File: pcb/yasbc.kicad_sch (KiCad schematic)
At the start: 173 parts, among them J1 BOOT, J10 Conn_02x20_Odd_Even, J2 USB TTY, J3 AudioJack3, J4 1V5, J5 3V3, J6 1V2, J7 USB DEV, J8 Micro_SD_Card, J9 USB HOST, Q1 AO3401A, Q2 AO3401A, SW1 RESET, SW2 SW_SPDT, SW3 SW_SPDT, SW4 SW_SPDT, SW5 SW_SPDT, SW6 SW_5WAY, U1 BCT2028, U3 Allwinner_A13, U4 CH340E, U5 TD6810, U6 SE5120, U7 K4B4G1646E, U8 MPU-6050, Y1 24M

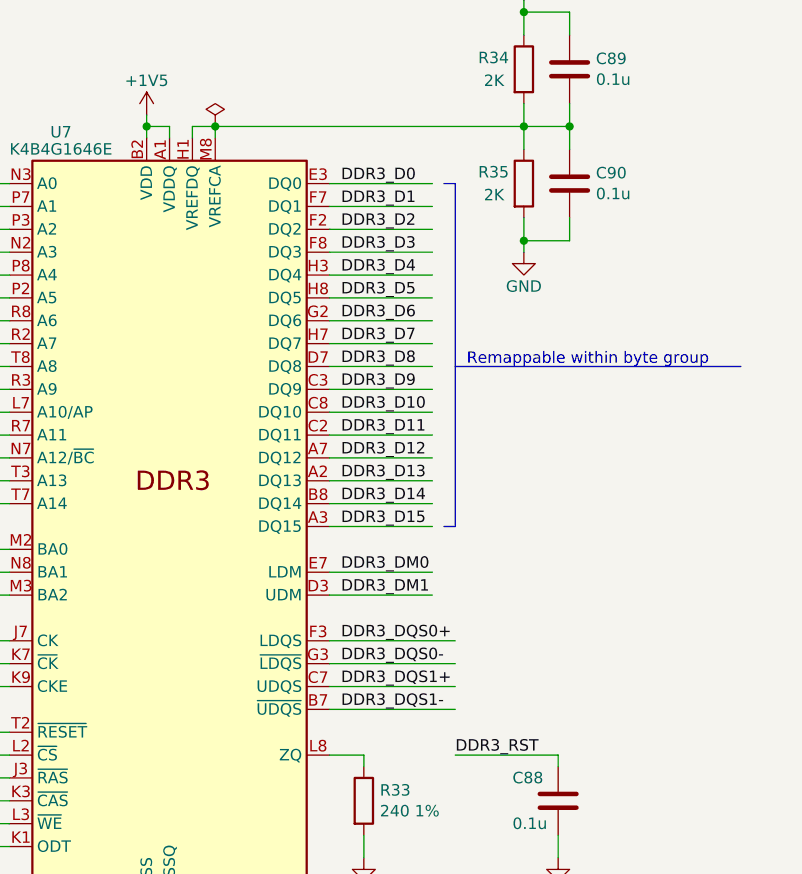
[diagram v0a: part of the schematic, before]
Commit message: Routed DDR3 data signals
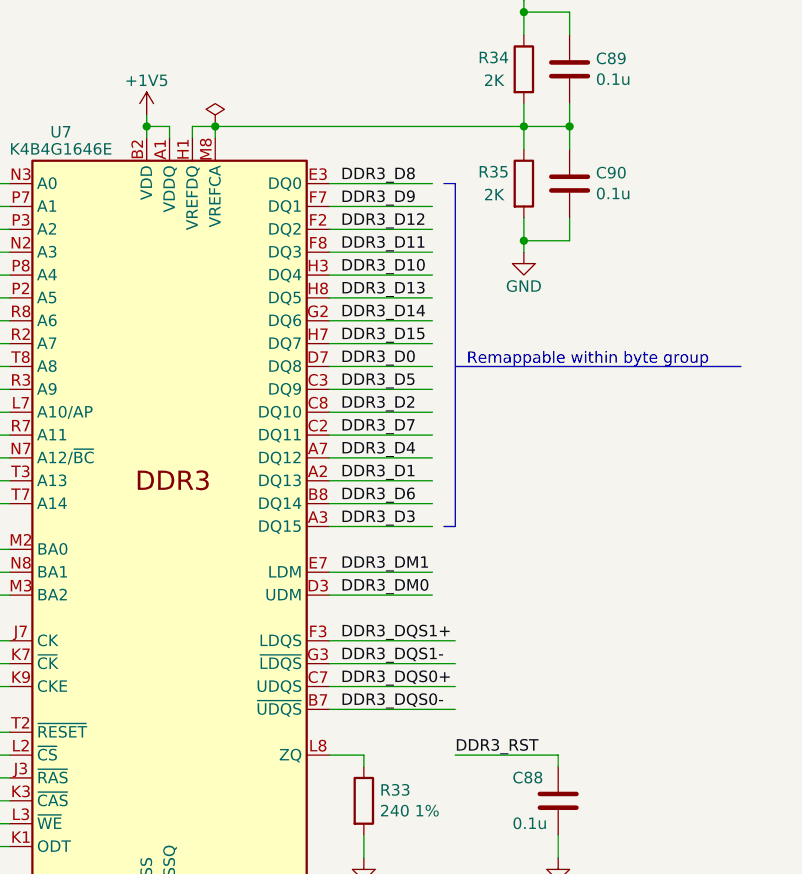
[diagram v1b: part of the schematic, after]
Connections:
- net DDR3_D0: now also U7.D7 (DQ8); no longer U7.E3 (DQ0)
- net DDR3_D1: now also U7.A2 (DQ13); no longer U7.F7 (DQ1)
- net DDR3_D10: now also U7.H3 (DQ4); no longer U7.C8 (DQ10)
- net DDR3_D11: now also U7.F8 (DQ3); no longer U7.C2 (DQ11)
- net DDR3_D12: now also U7.F2 (DQ2); no longer U7.A7 (DQ12)
- net DDR3_D13: now also U7.H8 (DQ5); no longer U7.A2 (DQ13)
- net DDR3_D14: now also U7.G2 (DQ6); no longer U7.B8 (DQ14)
- net DDR3_D15: now also U7.H7 (DQ7); no longer U7.A3 (DQ15)
- net DDR3_D2: now also U7.C8 (DQ10); no longer U7.F2 (DQ2)
- net DDR3_D3: now also U7.A3 (DQ15); no longer U7.F8 (DQ3)
- net DDR3_D4: now also U7.A7 (DQ12); no longer U7.H3 (DQ4)
- net DDR3_D5: now also U7.C3 (DQ9); no longer U7.H8 (DQ5)
- net DDR3_D6: now also U7.B8 (DQ14); no longer U7.G2 (DQ6)
- net DDR3_D7: now also U7.C2 (DQ11); no longer U7.H7 (DQ7)
- net DDR3_D8: now also U7.E3 (DQ0); no longer U7.D7 (DQ8)
- net DDR3_D9: now also U7.F7 (DQ1); no longer U7.C3 (DQ9)
- net DDR3_DM0: now also U7.D3 (UDM); no longer U7.E7 (LDM)
- net DDR3_DM1: now also U7.E7 (LDM); no longer U7.D3 (UDM)
- net DDR3_DQS0+: now also U7.C7 (UDQS); no longer U7.F3 (LDQS)
- net DDR3_DQS0-: now also U7.B7 (~{UDQS}); no longer U7.G3 (~{LDQS})
- net DDR3_DQS1+: now also U7.F3 (LDQS); no longer U7.C7 (UDQS)
- net DDR3_DQS1-: now also U7.G3 (~{LDQS}); no longer U7.B7 (~{UDQS})
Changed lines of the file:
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@@
   (no_connect (at 429.26 40.64))
   (no_connect (at 209.55 45.72))
-  (wire (pts (xy 533.4 71.12) (xy 544.83 71.12))
+  (wire (pts (xy 533.4 50.8) (xy 544.83 50.8))
     (stroke (width 0) (type default) (color 0 0 0 0))
   )
@@
     (stroke (width 0) (type default) (color 0 0 0 0))
   )
-  (wire (pts (xy 533.4 66.04) (xy 544.83 66.04))
+  (wire (pts (xy 533.4 45.72) (xy 544.83 45.72))
     (stroke (width 0) (type default) (color 0 0 0 0))
   )
@@
     (stroke (width 0) (type default) (color 0 0 0 0))
   )
-  (wire (pts (xy 533.4 96.52) (xy 547.37 96.52))
+  (wire (pts (xy 533.4 101.6) (xy 547.37 101.6))
     (stroke (width 0) (type default) (color 0 0 0 0))
   )
@@
     (stroke (width 0) (type default) (color 0 0 0 0))
   )
-  (wire (pts (xy 533.4 81.28) (xy 544.83 81.28))
+  (wire (pts (xy 533.4 60.96) (xy 544.83 60.96))
     (stroke (width 0) (type default) (color 0 0 0 0))
   )
@@
     (stroke (width 0) (type default) (color 0 0 0 0))
   )
-  (wire (pts (xy 533.4 60.96) (xy 544.83 60.96))
+  (wire (pts (xy 533.4 81.28) (xy 544.83 81.28))
     (stroke (width 0) (type default) (color 0 0 0 0))
   )
@@
     (stroke (width 0) (type default) (color 0 0 0 0))
   )
-  (wire (pts (xy 533.4 93.98) (xy 547.37 93.98))
+  (wire (pts (xy 533.4 99.06) (xy 547.37 99.06))
     (stroke (width 0) (type default) (color 0 0 0 0))
   )
@@
     (stroke (width 0) (type default) (color 0 0 0 0))
   )
-  (wire (pts (xy 533.4 55.88) (xy 544.83 55.88))
+  (wire (pts (xy 533.4 73.66) (xy 544.83 73.66))
     (stroke (width 0) (type default) (color 0 0 0 0))
   )
-  (wire (pts (xy 533.4 99.06) (xy 547.37 99.06))
+  (wire (pts (xy 533.4 93.98) (xy 547.37 93.98))
     (stroke (width 0) (type default) (color 0 0 0 0))
   )
@@
     (stroke (width 0) (type default) (color 0 0 0 0))
   )
-  (wire (pts (xy 533.4 78.74) (xy 544.83 78.74))
+  (wire (pts (xy 533.4 58.42) (xy 544.83 58.42))
     (stroke (width 0) (type default) (color 0 0 0 0))
   )
@@
     (stroke (width 0) (type default) (color 0 0 0 0))
   )
-  (wire (pts (xy 533.4 58.42) (xy 544.83 58.42))
+  (wire (pts (xy 533.4 78.74) (xy 544.83 78.74))
     (stroke (width 0) (type default) (color 0 0 0 0))
   )
@@
     (stroke (width 0) (type default) (color 0 0 0 0))
   )
-  (wire (pts (xy 533.4 76.2) (xy 544.83 76.2))
+  (wire (pts (xy 533.4 55.88) (xy 544.83 55.88))
     (stroke (width 0) (type default) (color 0 0 0 0))
   )
@@
     (stroke (width 0) (type default) (color 0 0 0 0))
   )
-  (wire (pts (xy 533.4 88.9) (xy 544.83 88.9))
+  (wire (pts (xy 533.4 86.36) (xy 544.83 86.36))
     (stroke (width 0) (type default) (color 0 0 0 0))
   )
@@
     (stroke (width 0) (type default) (color 0 0 0 0))
   )
-  (wire (pts (xy 533.4 48.26) (xy 544.83 48.26))
+  (wire (pts (xy 533.4 68.58) (xy 544.83 68.58))
     (stroke (width 0) (type default) (color 0 0 0 0))
   )
@@
     (stroke (width 0) (type default) (color 0 0 0 0))
   )
-  (wire (pts (xy 533.4 50.8) (xy 544.83 50.8))
+  (wire (pts (xy 533.4 71.12) (xy 544.83 71.12))
     (stroke (width 0) (type default) (color 0 0 0 0))
   )
@@
     (stroke (width 0) (type default) (color 0 0 0 0))
   )
-  (wire (pts (xy 533.4 101.6) (xy 547.37 101.6))
+  (wire (pts (xy 533.4 96.52) (xy 547.37 96.52))
     (stroke (width 0) (type default) (color 0 0 0 0))
   )
@@
     (stroke (width 0) (type default) (color 0 0 0 0))
   )
-  (wire (pts (xy 533.4 53.34) (xy 544.83 53.34))
+  (wire (pts (xy 533.4 76.2) (xy 544.83 76.2))
     (stroke (width 0) (type default) (color 0 0 0 0))
   )
@@
     (stroke (width 0) (type default) (color 0 0 0 0))
   )
-  (wire (pts (xy 533.4 45.72) (xy 544.83 45.72))
+  (wire (pts (xy 533.4 66.04) (xy 544.83 66.04))
     (stroke (width 0) (type default) (color 0 0 0 0))
   )
@@
     (stroke (width 0) (type default) (color 0 0 0 0))
   )
-  (wire (pts (xy 533.4 63.5) (xy 544.83 63.5))
+  (wire (pts (xy 533.4 43.18) (xy 544.83 43.18))
     (stroke (width 0) (type default) (color 0 0 0 0))
   )
@@
     (stroke (width 0) (type default) (color 0 0 0 0))
   )
-  (wire (pts (xy 533.4 68.58) (xy 544.83 68.58))
+  (wire (pts (xy 533.4 48.26) (xy 544.83 48.26))
     (stroke (width 0) (type default) (color 0 0 0 0))
   )
@@
     (stroke (width 0) (type default) (color 0 0 0 0))
   )
-  (wire (pts (xy 533.4 73.66) (xy 544.83 73.66))
+  (wire (pts (xy 533.4 53.34) (xy 544.83 53.34))
     (stroke (width 0) (type default) (color 0 0 0 0))
   )
@@
     (stroke (width 0) (type default) (color 0 0 0 0))
   )
-  (wire (pts (xy 533.4 43.18) (xy 544.83 43.18))
+  (wire (pts (xy 533.4 63.5) (xy 544.83 63.5))
     (stroke (width 0) (type default) (color 0 0 0 0))
   )
@@
     (stroke (width 0) (type default) (color 0 0 0 0))
   )
-  (wire (pts (xy 533.4 86.36) (xy 544.83 86.36))
+  (wire (pts (xy 533.4 88.9) (xy 544.83 88.9))
     (stroke (width 0) (type default) (color 0 0 0 0))
   )
@@
     (effects (font (size 1.27 1.27)) (justify left bottom))
   )
-  (label "DDR3_D13" (at 534.67 76.2 0)
+  (label "DDR3_D13" (at 534.67 55.88 0)
     (effects (font (size 1.27 1.27)) (justify left bottom))
   )
-  (label "DDR3_D3" (at 534.67 50.8 0)
+  (label "DDR3_D3" (at 534.67 81.28 0)
     (effects (font (size 1.27 1.27)) (justify left bottom))
   )
@@
     (effects (font (size 1.27 1.27)) (justify left bottom))
   )
-  (label "DDR3_D10" (at 534.67 68.58 0)
+  (label "DDR3_D10" (at 534.67 53.34 0)
     (effects (font (size 1.27 1.27)) (justify left bottom))
   )
@@
     (effects (font (size 1.27 1.27)) (justify left bottom))
   )
-  (label "DDR3_D2" (at 534.67 48.26 0)
+  (label "DDR3_D2" (at 534.67 68.58 0)
     (effects (font (size 1.27 1.27)) (justify left bottom))
   )
@@
     (effects (font (size 1.27 1.27)) (justify left bottom))
   )
-  (label "DDR3_D5" (at 534.67 55.88 0)
+  (label "DDR3_D5" (at 534.67 66.04 0)
     (effects (font (size 1.27 1.27)) (justify left bottom))
   )
@@
     (effects (font (size 1.27 1.27)) (justify left bottom))
   )
-  (label "DDR3_D4" (at 534.67 53.34 0)
+  (label "DDR3_D4" (at 534.67 73.66 0)
     (effects (font (size 1.27 1.27)) (justify left bottom))
   )
@@
     (effects (font (size 1.27 1.27)) (justify left bottom))
   )
-  (label "DDR3_D15" (at 534.67 81.28 0)
+  (label "DDR3_D15" (at 534.67 60.96 0)
     (effects (font (size 1.27 1.27)) (justify left bottom))
   )
@@
     (effects (font (size 1.27 1.27)) (justify left bottom))
   )
-  (label "DDR3_DQS1+" (at 534.67 99.06 0)
+  (label "DDR3_DQS1+" (at 534.67 93.98 0)
     (effects (font (size 1.27 1.27)) (justify left bottom))
   )
@@
     (effects (font (size 1.27 1.27)) (justify left bottom))
   )
-  (label "DDR3_DQS1-" (at 534.67 101.6 0)
+  (label "DDR3_DQS1-" (at 534.67 96.52 0)
     (effects (font (size 1.27 1.27)) (justify left bottom))
   )
@@
     (effects (font (size 1.27 1.27)) (justify left bottom))
   )
-  (label "DDR3_DM0" (at 534.67 86.36 0)
+  (label "DDR3_DM0" (at 534.67 88.9 0)
     (effects (font (size 1.27 1.27)) (justify left bottom))
   )
@@
     (effects (font (size 1.27 1.27)) (justify left bottom))
   )
-  (label "DDR3_D8" (at 534.67 63.5 0)
+  (label "DDR3_D8" (at 534.67 43.18 0)
     (effects (font (size 1.27 1.27)) (justify left bottom))
   )
@@
     (effects (font (size 1.27 1.27)) (justify left bottom))
   )
-  (label "DDR3_D14" (at 534.67 78.74 0)
+  (label "DDR3_D14" (at 534.67 58.42 0)
     (effects (font (size 1.27 1.27)) (justify left bottom))
   )
@@
     (effects (font (size 1.27 1.27)) (justify left bottom))
   )
-  (label "DDR3_D11" (at 534.67 71.12 0)
+  (label "DDR3_D11" (at 534.67 50.8 0)
     (effects (font (size 1.27 1.27)) (justify left bottom))
   )
-  (label "DDR3_D9" (at 534.67 66.04 0)
+  (label "DDR3_D9" (at 534.67 45.72 0)
     (effects (font (size 1.27 1.27)) (justify left bottom))
   )
-  (label "DDR3_D6" (at 534.67 58.42 0)
+  (label "DDR3_D6" (at 534.67 78.74 0)
     (effects (font (size 1.27 1.27)) (justify left bottom))
   )
@@
     (effects (font (size 1.27 1.27)) (justify left bottom))
   )
-  (label "DDR3_D1" (at 534.67 45.72 0)
+  (label "DDR3_D1" (at 534.67 76.2 0)
     (effects (font (size 1.27 1.27)) (justify left bottom))
   )
@@
     (effects (font (size 1.27 1.27)) (justify left bottom))
   )
-  (label "DDR3_DQS0+" (at 534.67 93.98 0)
+  (label "DDR3_DQS0+" (at 534.67 99.06 0)
     (effects (font (size 1.27 1.27)) (justify left bottom))
   )
@@
     (effects (font (size 1.27 1.27)) (justify right bottom))
   )
-  (label "DDR3_D0" (at 534.67 43.18 0)
+  (label "DDR3_D0" (at 534.67 63.5 0)
     (effects (font (size 1.27 1.27)) (justify left bottom))
   )
-  (label "DDR3_DQS0-" (at 534.67 96.52 0)
+  (label "DDR3_DQS0-" (at 534.67 101.6 0)
     (effects (font (size 1.27 1.27)) (justify left bottom))
   )
@@
     (effects (font (size 1.27 1.27)) (justify left bottom))
   )
-  (label "DDR3_D7" (at 534.67 60.96 0)
+  (label "DDR3_D7" (at 534.67 71.12 0)
     (effects (font (size 1.27 1.27)) (justify left bottom))
   )
@@
     (effects (font (size 1.27 1.27)) (justify left bottom))
   )
-  (label "DDR3_D12" (at 534.67 73.66 0)
+  (label "DDR3_D12" (at 534.67 48.26 0)
     (effects (font (size 1.27 1.27)) (justify left bottom))
   )
@@
     (effects (font (size 1.27 1.27)) (justify left bottom))
   )
-  (label "DDR3_DM1" (at 534.67 88.9 0)
+  (label "DDR3_DM1" (at 534.67 86.36 0)
     (effects (font (size 1.27 1.27)) (justify left bottom))
   )

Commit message: Worked on DDR3 decoupling caps
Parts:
- removed C83: 0.1u, Capacitor_SMD:C_0402_1005Metric, symbol Device:C
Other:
- moved on the sheet: C85, C86, C87, C91, C92, C93

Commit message: Cleaned up schematic
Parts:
- removed C10, C11, C12, C13, C15, C16, C17, C18, C21, C22, C23, C27, C3, C33, C34, C36, C37, C38, C4, C41, C42, C46, C47, C49, C50, C56, C58, C60, C61, C62, C7, C70, C72, C82, C88, C89, C9, C90: 0.1u, Capacitor_SMD:C_0603_1608Metric, symbol Device:C
- removed C14, C35, C40, C57, C63, C64, C65, C66, C67, C8: 10u, Capacitor_SMD:C_0603_1608Metric, symbol Device:C
- removed C2, C54, C55, C59, C68: 47u, Capacitor_SMD:C_0805_2012Metric, symbol Device:C
- removed C43, C51: 22p, Capacitor_SMD:C_0603_1608Metric, symbol Device:C
- removed C52: 1u, Capacitor_SMD:C_0603_1608Metric, symbol Device:C
- removed C69, C71, C73, C74, C75, C76, C77, C78, C79, C80, C81, C85, C86, C87, C91, C92, C93: 0.1u, Capacitor_SMD:C_0402_1005Metric, symbol Device:C
- removed C84: 0.1u 50V, Capacitor_SMD:C_0603_1608Metric, symbol Device:C
- removed J8: Micro_SD_Card, yasbc:microSD, symbol Connector:Micro_SD_Card
- removed RN1: 47K, Resistor_SMD:R_Array_Convex_4x0603, symbol Device:R_Pack04
- added C10, C11, C12, C13, C15, C16, C17, C18, C21, C22, C23, C27, C3, C33, C34, C36, C37, C38, C4, C41, C42, C46, C47, C49, C50, C56, C58, C60, C61, C62, C69, C7, C70, C71, C72, C73, C74, C75, C76, C77, C78, C79, C80, C81, C82, C85, C86, C87, C88, C89, C9, C90, C91, C92, C93: 100n, Capacitor_SMD:C_0603_1608Metric, symbol Device:C_Small
- added C14, C35, C40, C57, C63, C64, C65, C66, C67, C8: 10u, Capacitor_SMD:C_0603_1608Metric, symbol Device:C_Small
- added C2, C54, C55: 47u, Capacitor_SMD:C_0603_1608Metric, symbol Device:C_Small
- added C43, C51: 22p, Capacitor_SMD:C_0603_1608Metric, symbol Device:C_Small
- added C52: 1u, Capacitor_SMD:C_0603_1608Metric, symbol Device:C_Small
- added C59, C68: 47u, symbol Device:C_Small
- added C84: 100n 50V, Capacitor_SMD:C_0603_1608Metric, symbol Device:C_Small
- added R36, R37, R38, R39: 47K, Resistor_SMD:R_0603_1608Metric, symbol Device:R
- added U2: uSD_Card, yasbc:microSD, symbol yasbc:uSD_Card
- C20, C24, C26, C28: value 0.1u -> 100n
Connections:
- net +1V2: now also C11.1, C13.1, C16.1, C2.1, C22.1, C3.1, C34.1, C38.1, C4.1, C42.1, C47.1, C50.1, C55.1, C7.1, C9.1
- net +1V5: now also C33.1, C37.1, C41.1, C46.1, C49.1, C54.1, C60.1, C68.1, C69.1, C71.1, C73.1, C74.1, C75.1, C76.1, C77.1, C78.1, C79.1, C80.1, C81.1, C85.1, C86.1, C87.1, C89.1, C91.1, C92.1, C93.1
- net +3V3: now also C10.1, C12.1, C14.1, C15.1, C17.1, C21.1, C23.1, C27.2, C35.1, C58.1, C59.1, C70.1, C72.1, C8.1, R36.1, R37.1, R38.1, R39.1, U2.4 (VDD)
- net DDR3_RST: now also C88.1
- net GND: now also J10.40 (Pin_40), C10.2, C11.2, C12.2, C13.2, C14.2, C15.2, C16.2, C17.2, C18.2, C2.2, C21.2, C22.2, C23.2, C27.1, C3.2, C33.2, C34.2, C35.2, C36.2, C37.2, C38.2, C4.2, C40.2, C41.2, C42.2, C43.2, C46.2, C47.2, C49.2, C50.2, C51.2, C52.2, C54.2, C55.2, C56.2, C57.2, C58.2, C59.2, C61.2, C62.2, C63.2, C64.2, C65.2, C66.2, C67.2, C68.2, C69.2, C7.2, C70.2, C71.2, C72.2, C73.2, C74.2, C75.2, C76.2, C77.2, C78.2, C79.2, C8.2, C80.2, C81.2, C82.2, C84.2, C85.2, C86.2, C87.2, C88.2, C9.2, C90.2, C91.2, C92.2, C93.2, U2.6 (VSS), U2.9 (SHIELD)
- net RESET: now also C18.1
- net SD_CLK: now also U2.5 (CLK)
- net SD_CMD: now also R36.2, U2.3 (CMD)
- net SD_D0: now also R14.2, U2.7 (DAT0)
- net SD_D1: now also R39.2, U2.8 (DAT1); no longer R14.2
- net SD_D2: now also R38.2, U2.1 (DAT2)
- net SD_D3: now also R37.2, U2.2 (DAT3/CD)
- net SW_CENTER: now also C66.1
- net SW_DOWN: now also C63.1
- net SW_LEFT: now also C67.1
- net SW_R2R: now also C62.1
- net SW_RIGHT: now also C65.1
- net SW_UP: now also C64.1
- net USB_HOST_D+: no longer U3.96 (UDP1)
- net A13_SVREF: now reaches R18.2, R19.1, U3.18 (SVREF)
- net A13_SVREF: now also C60.2, C61.1
- net at U3.80 (VRP): now also C56.1, C57.1
- net at R13.1, U3.82 (VRA2): now also C36.1, C40.1
- net at U3.83 (VRA1): now also C52.1
- net at U3.91 (X24MOUT), Y1.1: now also C43.1
- net at U3.92 (X24MIN), Y1.3: now also C51.1
- net DDR3_REF: now reaches R34.2, R35.1, U7.H1 (VREFDQ), U7.M8 (VREFCA)
- net DDR3_REF: now also C89.2, C90.1
- net at U8.10 (REGOUT): now also C82.1
- net at U8.20 (CPOUT): now also C84.1
- no-connect marks 57 -> 35
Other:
- note added: "A13 [MISC]"
- note added: "A13 [MPU]"
- note added: "A13 [POWER]"
- note added: "ACCELEROMETER"
- note added: "BOOT SRC"
- note added: "CORE POWER"
- note added: "IO HEADER"
- note added: "IO POWER"
- note added: "IO [5 Way Switches]"
- note added: "IO [LEDs]"
- note added: "IO [R2R Switches]"
- note added: "MICRO SD CARD"
- note added: "MOUNTING HOLES"
- note added: "USB [DEV]"
- note added: "USB [HOST]"
- note added: "USB [UART DBG]"
- note removed: "A13 POWER/MISC"
- note removed: "DEBUG UART -> USB"
- note removed: "LEDs, Buttons & Switches"
- note removed: "USB Connectors"
- moved on the sheet: C1, C19, C20, C24, C25, C26, C28, C29, C30, C31, C32, C39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

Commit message: Further work on schematic
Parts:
- added C45, C53, C6, C83, C94, C95, C96, C97, C98, C99: 100n, Capacitor_SMD:C_0603_1608Metric, symbol Device:C_Small
- added J8: HDMI_A, symbol yasbc:HDMI_A
- added R40: 887, Resistor_SMD:R_0603_1608Metric, symbol Device:R_Small
- added U9: ADV7513, symbol yasbc:ADV7513
- C19, C31, C39: value 0.1u -> 100n
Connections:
- net +3V3: now also C99.1, U9.29 (DVDD_3V)
- net GND: now also C45.2, C53.2, C6.2, C83.2, C94.2, C95.2, C96.2, C97.2, C98.2, C99.2, J8.11 (CKS), J8.17 (GND), J8.2 (D2S), J8.5 (D1S), J8.8 (D0S), J8.SH, R40.1, U9.10 (LRCLK), U9.3 (SPDIF), U9.4 (MCLK), U9.43 (D[17]), U9.44 (D[16]), U9.5 (I2S0), U9.52 (D[9]), U9.54 (D[8]), U9.6 (I2S1), U9.61 (D[1]), U9.62 (D[0]), U9.7 (I2S2), U9.8 (I2S3), U9.9 (SCLK), U9.P (EPAD)
- net SW_DOWN: now also U3.7 (PC1/NALE/SPI0_MISO)
- net SW_LEFT: now also U3.6 (PC2/NCLE/SPI0_CLK)
- net SW_RIGHT: now also U3.3 (PC3/NCE1/SPI0_CS0)
- net SW_UP: now also U3.8 (PC0/NWE/SPI0_MOSI)
- net USB_HOST_D+: now also U3.96 (UDP1)
- net AD_PD: now reaches U3.103 (PB2/PWM/EINT16)
- net AD_PD: now also U9.22 (PD)
- net AD_SCL: now reaches U3.105 (PB15/TWI1_SCK)
- net AD_SCL: now also U9.35 (SCL)
- net AD_SDA: now reaches U3.106 (PB16/TWI1_SDA)
- net AD_SDA: now also U9.36 (SDA)
- net AD_VSYNC: now reaches U3.126 (PD27/LCD_VSYNC)
- net AD_VSYNC: now also U9.2 (VSYNC)
- net AD_HSYNC: now reaches U3.127 (PD26/LCD_HSYNC)
- net AD_HSYNC: now also U9.64 (HSYNC)
- net AD_DE: now reaches U3.128 (PD25/LCD_DE)
- net AD_DE: now also U9.63 (DE)
- net AD_CLK: now reaches U3.129 (PD24/LCD_CLK)
- net AD_CLK: now also U9.53 (CLK)
- net AD_D23: now reaches U3.130 (PD23/LCD_D23)
- net AD_D23: now also U9.37 (D[23])
- net AD_D22: now reaches U3.131 (PD22/LCD_D22)
- net AD_D22: now also U9.38 (D[22])
- net AD_D21: now reaches U3.132 (PD21/LCD_D21)
- net AD_D21: now also U9.39 (D[21])
- net AD_D20: now reaches U3.133 (PD20/LCD_D20)
- net AD_D20: now also U9.40 (D[20])
- net AD_D19: now reaches U3.134 (PD19/LCD_D19)
- net AD_D19: now also U9.41 (D[19])
- net AD_D18: now reaches U3.135 (PD18/LCD_D18)
- net AD_D18: now also U9.42 (D[18])
- net AD_D15: now reaches U3.136 (PD15/LCD_D15)
- net AD_D15: now also U9.45 (D[15])
- net AD_D14: now reaches U3.137 (PD14/LCD_D14)
- net AD_D14: now also U9.46 (D[14])
- net AD_D13: now reaches U3.138 (PD13/LCD_D13)
- net AD_D13: now also U9.47 (D[13])
- net AD_D12: now reaches U3.139 (PD12/LCD_D12)
- net AD_D12: now also U9.48 (D[12])
- net AD_D11: now reaches U3.140 (PD11/LCD_D11)
- net AD_D11: now also U9.49 (D[11])
- net AD_D10: now reaches U3.141 (PD10/LCD_D10)
- net AD_D10: now also U9.50 (D[10])
- net AD_D7: now reaches U3.143 (PD7/LCD_D7)
- net AD_D7: now also U9.55 (D[7])
- net AD_D6: now reaches U3.144 (PD6/LCD_D6)
- net AD_D6: now also U9.56 (D[6])
- net AD_D5: now reaches U3.145 (PD5/LCD_D5)
- net AD_D5: now also U9.57 (D[5])
- net AD_D4: now reaches U3.146 (PD4/LCD_D4)
- net AD_D4: now also U9.58 (D[4])
- net AD_D3: now reaches U3.147 (PD3/LCD_D3)
- net AD_D3: now also U9.59 (D[3])
- net AD_D2: now reaches U3.148 (PD2/LCD_D2)
- net AD_D2: now also U9.60 (D[2])
- net AD_INT: now reaches U3.150 (PB3/IR_TX/EINT17)
- net AD_INT: now also U9.28 (INT)
- net VBUS renamed +5V
- net +5V: now also J8.18 (+5V)
- new net: R40.2, U9.14 (R_EXT)
- new net +1V8: C45.1, C53.1, C6.1, C83.1, C94.1, C95.1, C96.1, C97.1, C98.1, U9.1 (DVDD), U9.11 (DVDD), U9.12 (PVDD), U9.13 (BGVDD), U9.15 (AVDD), U9.19 (AVDD), U9.25 (AVDD), U9.31 (DVDD), U9.51 (DVDD)
- new net AD_O_CEC: J8.13 (CEC), U9.30 (CEC)
- new net AD_O_HPD: J8.19 (HPD), U9.16 (HPD)
- new net AD_O_SCL: J8.15 (SCL), U9.33 (DDCSCL)
- new net AD_O_SDA: J8.16 (SDA), U9.34 (DDCSDA)
- new net AD_O_TX0_N: J8.9 (D0-), U9.20 (TX0_N)
- new net AD_O_TX0_P: J8.7 (D0+), U9.21 (TX0_P)
- new net AD_O_TX1_N: J8.6 (D1-), U9.23 (TX1_N)
- new net AD_O_TX1_P: J8.4 (D1+), U9.24 (TX1_P)
- new net AD_O_TX2_N: J8.3 (D2-), U9.26 (TX2_N)
- new net AD_O_TX2_P: J8.1 (D2+), U9.27 (TX2_P)
- new net AD_O_TXC_N: J8.12 (CK-), U9.17 (TXC_N)
- new net AD_O_TXC_P: J8.10 (CK+), U9.18 (TXC_P)
- no-connect marks 35 -> 44
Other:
- note added: "<- CEC CLK Not Required?"
- note added: "AVDD Decoupling"
- note added: "BGVDD Decoupling"
- note added: "DVDD Decoupling"
- note added: "HDMI TRANSMITTER"
- note added: "POWER SUPPLY (5V)"
- note added: "PVDD Decoupling"
- moved on the sheet: C18, C20, C24, C26, C28, C30, C43, C51, F1, J1, J3, J9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
